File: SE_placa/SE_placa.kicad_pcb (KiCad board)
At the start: 2 copper layers, 114.3 x 57.4 mm, 70 parts, among them IC1 TP4056, J1 5V, J2 Micro_SD_Card_Det_Hirose_DM3AT, J3 Conn_02x07_ESP32_IO, J4 I2C-0, J5 I2C-1, J6 Conn_02x03_LORA_IO, J7 U.FL-R-SMT(01), J8 UART, J9 Connector Bateria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

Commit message: Update SE_placa.kicad_pcb
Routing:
- net /cargador_regulador/BAT+: track 51.7 -> 53.0 mm
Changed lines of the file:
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@@
     (thickness 1.6)
     (drawings 4)
-    (tracks 397)
+    (tracks 398)
     (zones 0)
     (modules 70)
@@
   )
   (setup
-    (last_trace_width 1)
+    (last_trace_width 0.3)
     (user_trace_width 0.3)
     (user_trace_width 1)
@@
   (segment (start 122.408 31.008) (end 122.174 31.242) (width 0.3) (layer F.Cu) (net 50))
   (via (at 122.174 31.242) (size 0.8) (drill 0.4) (layers F.Cu B.Cu) (net 50))
-  (segment (start 127.508 31.242) (end 130.81 34.544) (width 0.3) (layer B.Cu) (net 50))
-  (segment (start 122.174 31.242) (end 127.508 31.242) (width 0.3) (layer B.Cu) (net 50))
   (segment (start 125.97325 39.12675) (end 130.556 34.544) (width 1) (layer B.Cu) (net 50))
   (segment (start 130.556 34.544) (end 130.81 34.544) (width 1) (layer B.Cu) (net 50))
   (via (at 130.81 34.544) (size 1.8) (drill 1.4) (layers F.Cu B.Cu) (net 50))
+  (segment (start 123.19 34.544) (end 130.81 34.544) (width 0.3) (layer B.Cu) (net 50))
+  (segment (start 122.174 33.528) (end 123.19 34.544) (width 0.3) (layer B.Cu) (net 50))
+  (segment (start 122.174 31.242) (end 122.174 33.528) (width 0.3) (layer B.Cu) (net 50))
   (segment (start 132.588 36.989) (end 132.62 36.957) (width 0.3) (layer F.Cu) (net 51))
   (segment (start 132.588 37.084) (end 132.588 36.989) (width 0.3) (layer F.Cu) (net 51))
@@
   (segment (start 128.778 39.667) (end 130.005 40.894) (width 1) (layer F.Cu) (net 73))
   (segment (start 128.778 33.782) (end 128.778 39.667) (width 1) (layer F.Cu) (net 73))
-  (segment (start 128.004 33.008) (end 128.778 33.782) (width 1) (layer F.Cu) (net 73))
   (segment (start 126.976 33.008) (end 128.004 33.008) (width 0.3) (layer F.Cu) (net 73))
   (segment (start 136.62 41.688) (end 136.62 40.894) (width 1) (layer F.Cu) (net 73))
@@
   (segment (start 131.826 43.942) (end 130.005 42.121) (width 1) (layer F.Cu) (net 73))
   (segment (start 134.611 43.942) (end 131.826 43.942) (width 1) (layer F.Cu) (net 73))
+  (segment (start 128.004 33.008) (end 128.778 33.782) (width 0.3) (layer F.Cu) (net 73))
   (segment (start 131.108 31.508) (end 132.62 33.02) (width 0.3) (layer F.Cu) (net 74))
   (segment (start 126.976 31.508) (end 131.108 31.508) (width 0.3) (layer F.Cu) (net 74))

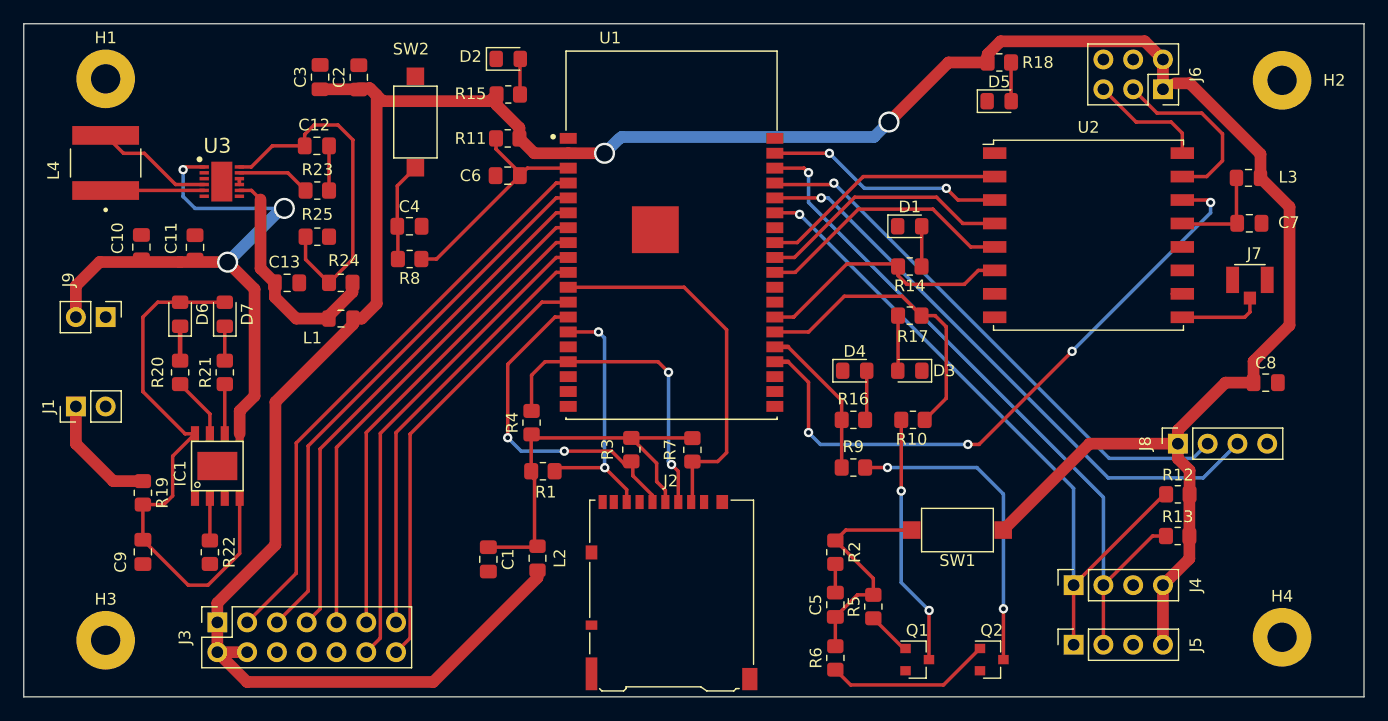
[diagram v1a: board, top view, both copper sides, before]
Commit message: Ruteo y vias
Se pusieron zonas para agrandar los caminos falta poner las capas de tierra
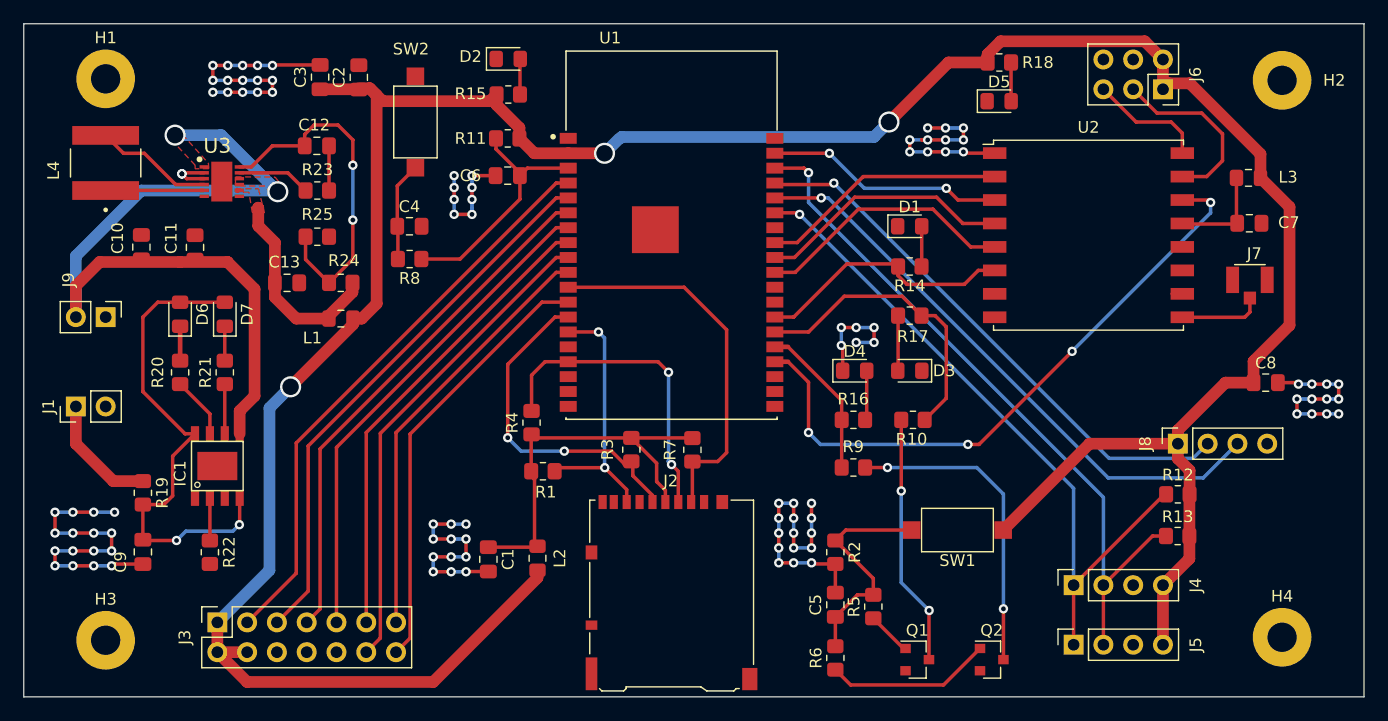
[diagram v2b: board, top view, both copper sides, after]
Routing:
- net GND: track 4.71 -> 147.0 mm, vias 0 -> 97
- net /cargador_regulador/BAT+: track 53.0 -> 68.1 mm, vias 3 -> 2
- net Net-(C9-Pad1): track 47.4 -> 42.8 mm, vias 0 -> 2
- net /cargador_regulador/Vout3.3V: track 20.2 -> 17.5 mm
- net +3V3: track 250.1 -> 251.3 mm, vias 2 -> 3
- net /ESP-EN: track 20.1 -> 21.3 mm
- net /cargador_regulador/FB: vias 0 -> 2
- added copper zone on F.Cu, net /cargador_regulador/BAT+
- added copper zone on F.Cu, net /cargador_regulador/Vout3.3V

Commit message: Update SE_placa.kicad_pcb
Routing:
- added copper zone on B.Cu, net GND
- added copper zone on F.Cu, net GND
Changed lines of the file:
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@@
     (thickness 1.6)
     (drawings 4)
-    (tracks 615)
+    (tracks 616)
     (zones 0)
     (modules 70)
@@
   (via (at 114.554 60.452) (size 0.8) (drill 0.4) (layers F.Cu B.Cu) (net 1))
   (segment (start 112.776 60.452) (end 114.554 60.452) (width 0.3) (layer F.Cu) (net 1))
-  (via (at 116.332 60.452) (size 0.8) (drill 0.4) (layers F.Cu B.Cu) (net 1))
-  (segment (start 114.554 60.452) (end 116.332 60.452) (width 0.3) (layer B.Cu) (net 1))
   (via (at 178.308 46.228) (size 0.8) (drill 0.4) (layers F.Cu B.Cu) (net 1))
   (segment (start 178.426 46.346) (end 178.308 46.228) (width 0.3) (layer F.Cu) (net 1))
@@
   (segment (start 122.4828 32.008) (end 122.0724 31.5976) (width 0.3) (layer F.Cu) (net 1))
   (segment (start 123.976 32.008) (end 122.4828 32.008) (width 0.3) (layer F.Cu) (net 1))
+  (via (at 116.0399 60.4647) (size 0.8) (drill 0.4) (layers F.Cu B.Cu) (net 1))
+  (segment (start 114.554 60.452) (end 116.0272 60.452) (width 0.3) (layer B.Cu) (net 1))
+  (segment (start 116.0272 60.452) (end 116.0399 60.4647) (width 0.3) (layer B.Cu) (net 1))
   (segment (start 151.8605 53.8475) (end 151.892 53.816) (width 0.4) (layer F.Cu) (net 2))
   (segment (start 151.8605 56.9595) (end 151.8605 53.8475) (width 0.3) (layer F.Cu) (net 2))
@@
   )
   (zone (net 50) (net_name /cargador_regulador/BAT+) (layer F.Cu) (hatch edge 0.508)
+    (priority 1)
     (connect_pads yes (clearance 0.2))
     (min_thickness 0.2)
@@
   )
   (zone (net 73) (net_name /cargador_regulador/Vout3.3V) (layer F.Cu) (hatch edge 0.508)
+    (priority 1)
     (connect_pads yes (clearance 0.2))
     (min_thickness 0.2)
@@
   )
   (zone (net 50) (net_name /cargador_regulador/BAT+) (layer F.Cu) (hatch edge 0.508)
+    (priority 1)
     (connect_pads yes (clearance 0.2))
     (min_thickness 0.2)
@@
     (polygon
       (pts
-        (xy 124.333 30.6959) (xy 124.3711 31.1531) (xy 123.2027 31.1658) (xy 123.2027 30.861) (xy 120.777 28.2575)
+        (xy 124.333 30.6959) (xy 124.3711 31.1531) (xy 123.4567 31.1277) (xy 123.2027 30.861) (xy 120.777 28.2575)
         (xy 121.5644 27.6225)
       )
     )
+  )
+  (zone (net 1) (net_name GND) (layer F.Cu) (hatch edge 0.508)
+    (connect_pads yes (clearance 0.2))
+    (min_thickness 0.2)
+    (fill yes (arc_segments 32) (thermal_gap 0.508) (thermal_bridge_width 0.508))
+    (polygon
+      (pts
+        (xy 222.885 18.796) (xy 222.885 76.2) (xy 108.585 76.1873) (xy 108.5977 18.7833)
+      )
+    )
+  )
+  (zone (net 1) (net_name GND) (layer B.Cu) (hatch edge 0.508)
+    (connect_pads yes (clearance 0.2))
+    (min_thickness 0.2)
+    (fill yes (arc_segments 32) (thermal_gap 0.508) (thermal_bridge_width 0.508))
+    (polygon
+      (pts
+        (xy 222.885 76.2) (xy 108.585 76.2) (xy 108.585 18.796) (xy 222.885 18.796)
+      )
+    )

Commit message: Update SE_placa.kicad_pcb
Organizando los nombres de los componentes  para que se puedan leer
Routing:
- net GND: track 146.7 -> 142.1 mm, vias 97 -> 95

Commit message: Gerber files
Generacion de archivos gerber
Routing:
- net GND: track 142.1 -> 337.1 mm, vias 95 -> 214
